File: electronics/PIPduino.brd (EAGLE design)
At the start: 46 x 46 mm, 45 parts, among them IC1 ATmega328P\, J1 ISP|SPI, U1 NCP5500, X1 16MHz

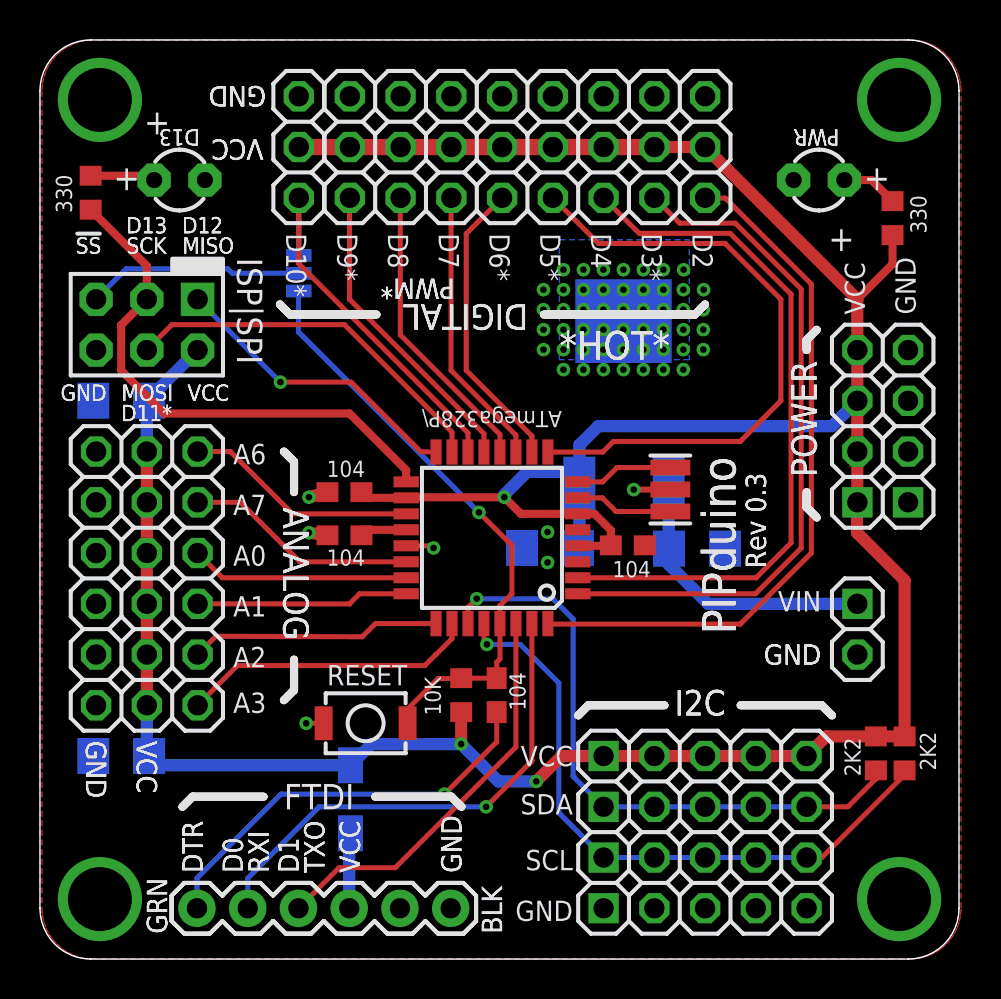
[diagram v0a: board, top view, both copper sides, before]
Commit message: minor silk corrections, moved D13/PWR labels, corrected 40cm->40mm, updated 3mm LED pkg + sign
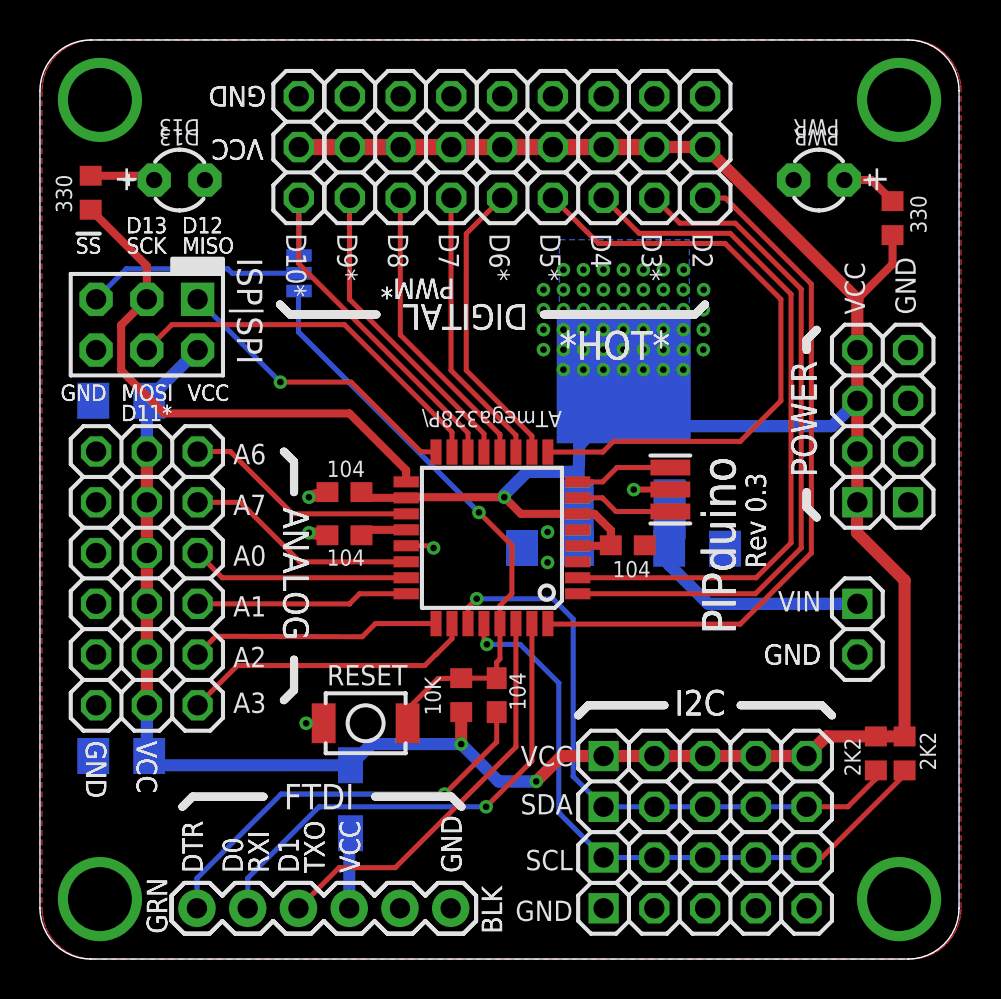
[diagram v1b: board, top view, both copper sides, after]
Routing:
- net N$2: track 14.1 -> 13.0 mm
- net VCC: track 162.5 -> 163.6 mm
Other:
- board text added: "Holes on 40mm square"
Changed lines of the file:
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@@
 <layer number="54" name="bPadExt" color="1" fill="1" visible="no" active="no"/>
 <layer number="56" name="wert" color="7" fill="1" visible="no" active="no"/>
+<layer number="57" name="tCAD" color="7" fill="1" visible="no" active="no"/>
+<layer number="59" name="tCarbon" color="7" fill="1" visible="no" active="no"/>
+<layer number="60" name="bCarbon" color="7" fill="1" visible="no" active="no"/>
+<layer number="90" name="Modules" color="5" fill="1" visible="no" active="no"/>
 <layer number="91" name="Nets" color="2" fill="1" visible="no" active="no"/>
 <layer number="92" name="Busses" color="1" fill="1" visible="no" active="no"/>
@@
 <layer number="97" name="Info" color="7" fill="1" visible="no" active="no"/>
 <layer number="98" name="Guide" color="6" fill="1" visible="no" active="no"/>
+<layer number="99" name="SpiceOrder" color="7" fill="1" visible="no" active="no"/>
 <layer number="100" name="NonViaHole" color="14" fill="1" visible="no" active="yes"/>
 <layer number="101" name="PlacementGuide" color="7" fill="1" visible="no" active="yes"/>
@@
 <layer number="108" name="tplace-old" color="10" fill="1" visible="no" active="yes"/>
 <layer number="109" name="ref-old" color="11" fill="1" visible="no" active="yes"/>
+<layer number="110" name="fp0" color="7" fill="1" visible="no" active="yes"/>
+<layer number="111" name="LPC17xx" color="7" fill="1" visible="no" active="yes"/>
+<layer number="112" name="tSilk" color="7" fill="1" visible="yes" active="yes"/>
+<layer number="113" name="IDFDebug" color="4" fill="1" visible="no" active="yes"/>
 <layer number="116" name="Patch_BOT" color="9" fill="4" visible="no" active="yes"/>
 <layer number="121" name="tsilk" color="14" fill="1" visible="no" active="yes"/>
 <layer number="122" name="bsilk" color="6" fill="1" visible="no" active="yes"/>
+<layer number="123" name="tTestmark" color="7" fill="1" visible="no" active="yes"/>
+<layer number="124" name="bTestmark" color="7" fill="1" visible="no" active="yes"/>
 <layer number="125" name="_tNames" color="7" fill="1" visible="no" active="yes"/>
+<layer number="126" name="_bNames" color="7" fill="1" visible="no" active="yes"/>
+<layer number="127" name="_tValues" color="7" fill="1" visible="no" active="yes"/>
+<layer number="128" name="_bValues" color="7" fill="1" visible="no" active="yes"/>
+<layer number="129" name="Mask" color="7" fill="1" visible="no" active="yes"/>
+<layer number="131" name="tAdjust" color="7" fill="1" visible="no" active="yes"/>
+<layer number="132" name="bAdjust" color="7" fill="1" visible="no" active="yes"/>
 <layer number="144" name="Drill_legend" color="7" fill="1" visible="no" active="yes"/>
+<layer number="150" name="Notes" color="7" fill="1" visible="no" active="yes"/>
 <layer number="151" name="HeatSink" color="7" fill="1" visible="no" active="yes"/>
+<layer number="152" name="_bDocu" color="7" fill="1" visible="no" active="yes"/>
+<layer number="153" name="FabDoc1" color="7" fill="1" visible="no" active="yes"/>
+<layer number="154" name="FabDoc2" color="7" fill="1" visible="no" active="yes"/>
+<layer number="155" name="FabDoc3" color="7" fill="1" visible="no" active="yes"/>
 <layer number="199" name="Contour" color="7" fill="1" visible="no" active="yes"/>
 <layer number="200" name="200bmp" color="1" fill="10" visible="no" active="yes"/>
@@
 <layer number="223" name="223bmp" color="24" fill="1" visible="no" active="no"/>
 <layer number="224" name="224bmp" color="25" fill="1" visible="no" active="no"/>
+<layer number="225" name="225bmp" color="7" fill="1" visible="no" active="yes"/>
+<layer number="226" name="226bmp" color="7" fill="1" visible="no" active="yes"/>
+<layer number="227" name="227bmp" color="7" fill="1" visible="no" active="yes"/>
+<layer number="228" name="228bmp" color="7" fill="1" visible="no" active="yes"/>
+<layer number="229" name="229bmp" color="7" fill="1" visible="no" active="yes"/>
+<layer number="230" name="230bmp" color="7" fill="1" visible="no" active="yes"/>
 <layer number="231" name="Eagle3D_PG1" color="14" fill="1" visible="no" active="yes"/>
 <layer number="232" name="Eagle3D_PG2" color="14" fill="2" visible="no" active="yes"/>
 <layer number="233" name="Eagle3D_PG3" color="14" fill="4" visible="no" active="yes"/>
+<layer number="248" name="Housing" color="7" fill="1" visible="no" active="yes"/>
+<layer number="249" name="Edge" color="7" fill="1" visible="no" active="yes"/>
 <layer number="250" name="Descript" color="7" fill="1" visible="no" active="yes"/>
 <layer number="251" name="SMDround" color="7" fill="1" visible="no" active="yes"/>
 <layer number="254" name="OrgLBR" color="7" fill="1" visible="no" active="yes"/>
+<layer number="255" name="routoute" color="7" fill="1" visible="no" active="yes"/>
 </layers>
 <board>
@@
 <text x="37.074" y="14.131" size="1.27" layer="26" font="vector" ratio="12" rot="MR0">Put In Project</text>
 <text x="10.416" y="43.42" size="1.016" layer="28" font="vector" ratio="12" rot="MR0">#4/M3</text>
-<text x="23.929" y="44.685" size="1.016" layer="28" font="vector" ratio="12" rot="MR0">Holes on 40cm square</text>
+<text x="23.929" y="44.685" size="1.016" layer="28" font="vector" ratio="12" rot="MR0">Holes on 40mm square</text>
 <text x="11.706" y="33.786" size="1.016" layer="26" font="vector" ratio="12" rot="MR0">!SS</text>
 <text x="3.505" y="34.3" size="1.016" layer="26" font="vector" ratio="12" rot="MR0">!SS</text>
@@
 </element>
 <element name="D13" library="bt_opto" package="LED3MM" value="" x="6.985" y="38.989" smashed="yes">
-<attribute name="NAME" x="8.001" y="41.529" size="0.8128" layer="25" font="vector" ratio="12" rot="SR180"/>
+<attribute name="NAME" x="8.001" y="42.037" size="0.8128" layer="25" font="vector" ratio="12" rot="SR180"/>
 <attribute name="VALUE" x="8.89" y="37.338" size="1.27" layer="27" ratio="10"/>
 </element>
 <element name="PWR" library="bt_opto" package="LED3MM" value="" x="38.989" y="38.989" smashed="yes" rot="R180">
-<attribute name="NAME" x="40.005" y="41.529" size="0.8128" layer="25" font="vector" ratio="12" rot="SR180"/>
+<attribute name="NAME" x="40.005" y="42.037" size="0.8128" layer="25" font="vector" ratio="12" rot="SR180"/>
 <attribute name="VALUE" x="37.084" y="40.64" size="1.27" layer="27" ratio="10" rot="R180"/>
 </element>
@@
 <contactref element="U1" pad="1"/>
 <wire x1="40.91" y1="17.78" x2="33.443" y2="17.78" width="0.6096" layer="16"/>
-<wire x1="31.4706" y1="23.6474" x2="31.4706" y2="21.5764" width="0.6096" layer="16"/>
+<wire x1="31.51" y1="22.505" x2="31.4706" y2="21.5764" width="0.6096" layer="16"/>
 <wire x1="31.4706" y1="21.5764" x2="31.489" y2="20.542" width="0.6096" layer="16"/>
 <wire x1="33.443" y1="17.78" x2="31.489" y2="19.734" width="0.6096" layer="16"/>
@@
 <contactref element="U1" pad="3"/>
 <contactref element="C2" pad="1"/>
-<wire x1="27.0002" y1="23.6474" x2="27.0002" y2="21.6632" width="0.6096" layer="16"/>
+<wire x1="26.91" y1="22.505" x2="27.0002" y2="21.6632" width="0.6096" layer="16"/>
 <wire x1="27.0002" y1="21.6632" x2="26.927" y2="20.574" width="0.6096" layer="16"/>
 <wire x1="23.241" y1="23.114" x2="23.241" y2="23.241" width="0.6096" layer="16"/>
 <wire x1="23.241" y1="23.241" x2="24.384" y2="24.384" width="0.6096" layer="16"/>
 <wire x1="24.384" y1="24.384" x2="26.7208" y2="24.384" width="0.6096" layer="16"/>
-<wire x1="26.7208" y1="24.384" x2="27.0002" y2="23.6474" width="0.6096" layer="16"/>
+<wire x1="26.7208" y1="24.384" x2="26.91" y2="22.505" width="0.6096" layer="16"/>
 <wire x1="23.241" y1="23.114" x2="18.669" y2="23.114" width="0.4064" layer="1"/>
-<wire x1="27.0002" y1="23.6474" x2="27.0002" y2="25.7302" width="0.6096" layer="16"/>
+<wire x1="26.91" y1="22.505" x2="27.0002" y2="25.7302" width="0.6096" layer="16"/>
 <wire x1="27.0002" y1="25.7302" x2="27.94" y2="26.67" width="0.6096" layer="16"/>
 <wire x1="27.94" y1="26.67" x2="39.64" y2="26.67" width="0.6096" layer="16"/>

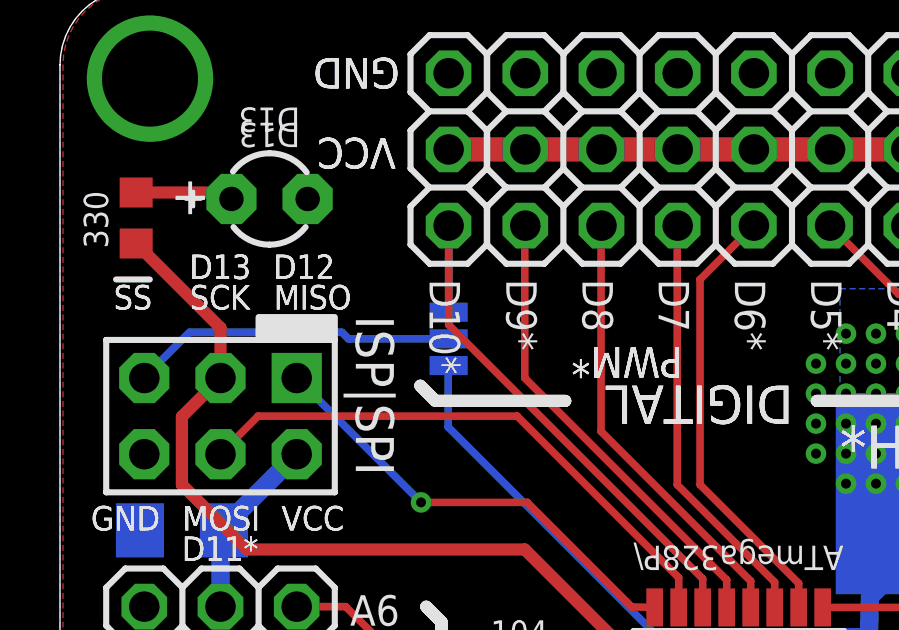
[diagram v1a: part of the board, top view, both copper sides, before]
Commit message: Updated 3-way jumper selector
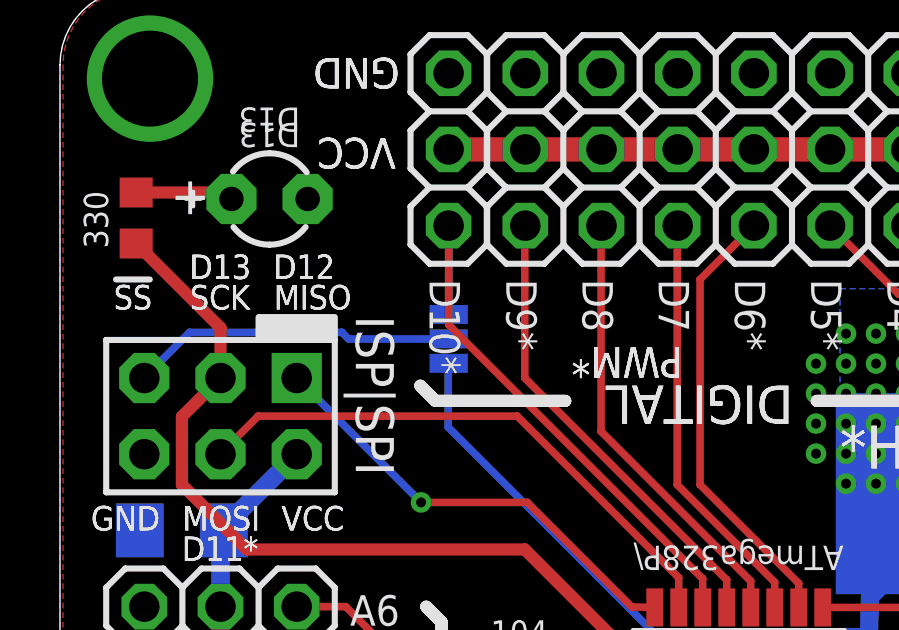
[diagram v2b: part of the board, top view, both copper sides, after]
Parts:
- SJ1: device SparkFun-Passives:SJ_3 -> SparkFun-Passives:PAD-JUMPER-3-2OF3_NC_BY_PASTE_YES_SILK_FULL_BOX
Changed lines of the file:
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@@
 <attribute name="VALUE" x="35.56" y="19.632" size="0.8128" layer="28" font="vector" ratio="12" rot="MR90"/>
 </element>
-<element name="SJ1" library="SparkFun-Passives" package="SJ_3" value="" x="12.956" y="34.324" smashed="yes" rot="MR90">
+<element name="SJ1" library="SparkFun-Passives" package="PAD-JUMPER-3-2OF3_NC_BY_PASTE_YES_SILK_FULL_BOX" value="" x="12.956" y="34.324" smashed="yes" rot="MR90">
 <attribute name="VALUE" x="12.956" y="34.2239" size="0.02" layer="28" rot="MR90"/>
 <attribute name="VALUE" x="11.051" y="33.054" size="0.4064" layer="28" rot="MR90"/>
@@
 <contactref element="SJ1" pad="3"/>
 <contactref element="JP2" pad="1"/>
-<wire x1="12.956" y1="35.213" x2="12.956" y2="36.998" width="0.254" layer="16"/>
+<wire x1="12.956" y1="35.1368" x2="12.956" y2="36.998" width="0.254" layer="16"/>
 <wire x1="12.956" y1="36.998" x2="12.954" y2="38.1" width="0.254" layer="16"/>
 <wire x1="12.954" y1="38.1" x2="12.954" y2="34.798" width="0.254" layer="1"/>
@@
 <wire x1="21.971" y1="22.352" x2="12.94" y2="31.383" width="0.254" layer="16"/>
 <wire x1="12.94" y1="31.383" x2="12.94" y2="33.419" width="0.254" layer="16"/>
-<wire x1="12.94" y1="33.419" x2="12.956" y2="33.435" width="0.254" layer="16"/>
+<wire x1="12.94" y1="33.419" x2="12.956" y2="33.5112" width="0.254" layer="16"/>
 <wire x1="21.082" y1="14.058" x2="19.922" y2="14.034" width="0.254" layer="1"/>
 <wire x1="19.922" y1="14.034" x2="18.415" y2="12.527" width="0.254" layer="1"/>
